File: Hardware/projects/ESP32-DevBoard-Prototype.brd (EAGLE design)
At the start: 88.1 x 80 mm, 37 parts

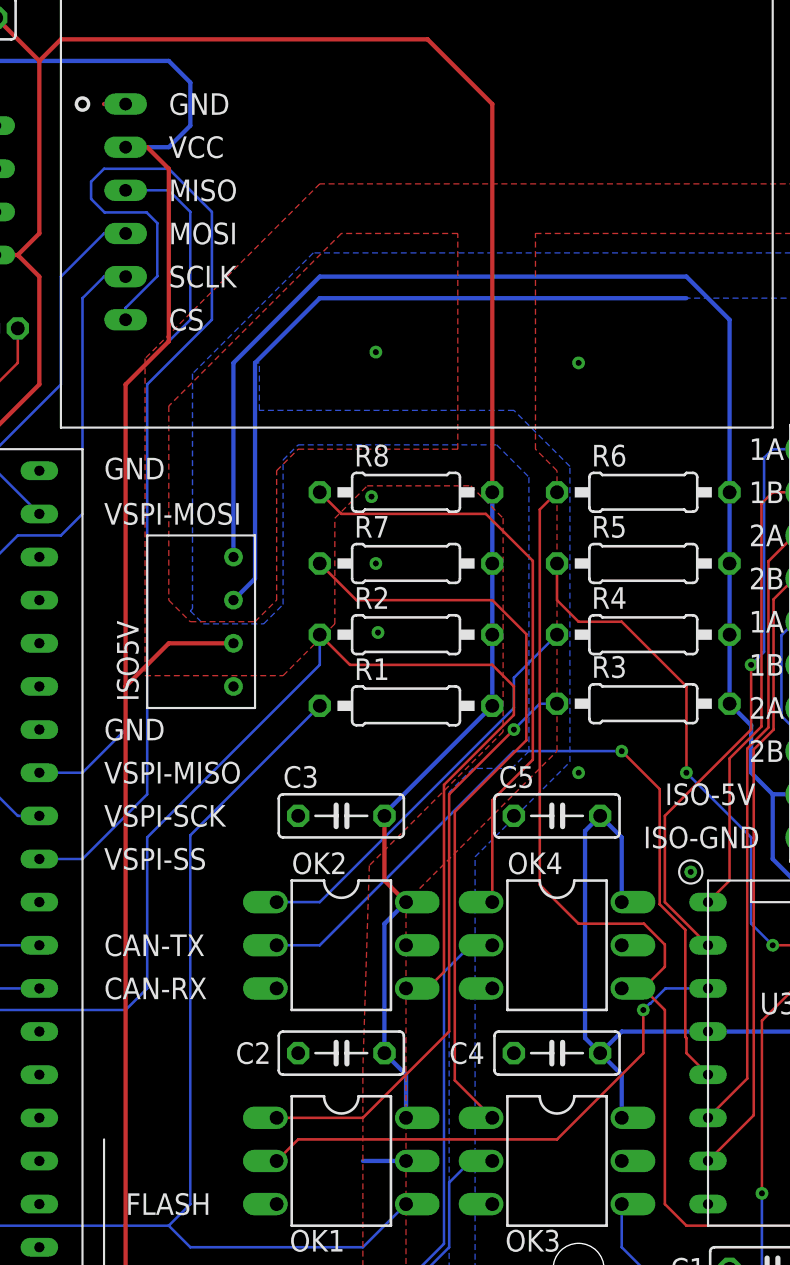
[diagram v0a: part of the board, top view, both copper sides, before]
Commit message: Updated board for ESP32 dev-board hardware to remove unnecessary traces.
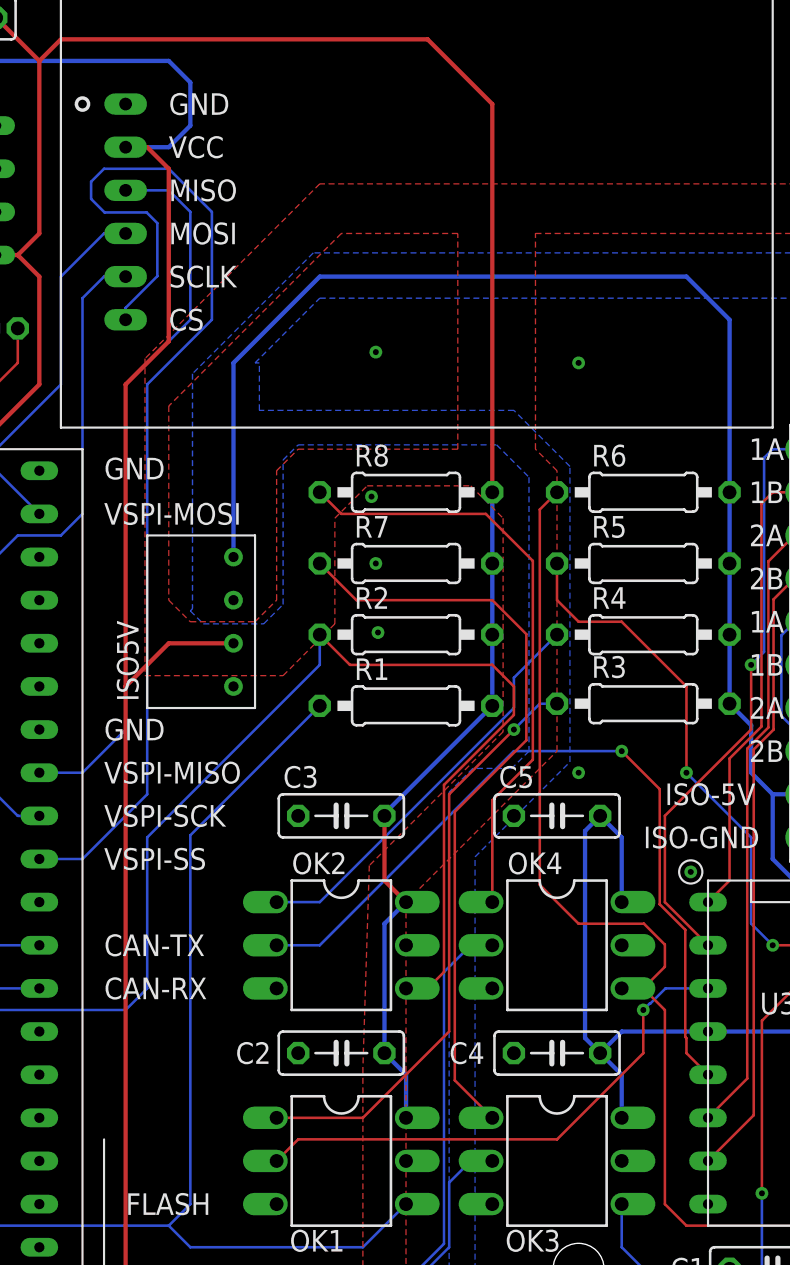
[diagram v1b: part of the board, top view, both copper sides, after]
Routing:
- net ISO_GND: track 41.5 -> 0.00 mm
- net GND: track 3.81 -> 0.00 mm
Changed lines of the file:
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@@
 <drawing>
 <settings>
-<setting alwaysvectorfont="yes"/>
+<setting alwaysvectorfont="no"/>
 <setting verticaltext="up"/>
 </settings>
@@
 <contactref element="LED2" pad="K"/>
 <contactref element="LED3" pad="K"/>
-<wire x1="41.91" y1="71.12" x2="43.18" y2="71.12" width="0.254" layer="1"/>
 <contactref element="C3" pad="1"/>
 <contactref element="C2" pad="1"/>
 <contactref element="ISO5V" pad="1"/>
-<wire x1="57.15" y1="8.89" x2="59.69" y2="8.89" width="0.254" layer="16"/>
 <polygon width="0.254" layer="16">
 <vertex x="0" y="0"/>
@@
 <via x="69.85" y="55.88" extent="1-16" drill="0.35"/>
 <via x="85.979" y="34.544" extent="1-16" drill="0.35"/>
-<wire x1="49.53" y1="41.91" x2="50.8" y2="43.18" width="0.254" layer="16"/>
-<wire x1="50.8" y1="43.18" x2="50.8" y2="55.88" width="0.254" layer="16"/>
-<wire x1="50.8" y1="55.88" x2="54.61" y2="59.69" width="0.254" layer="16"/>
-<wire x1="54.61" y1="59.69" x2="76.2" y2="59.69" width="0.254" layer="16"/>
 <polygon width="0.254" layer="1">
 <vertex x="59.69" y="0"/>
